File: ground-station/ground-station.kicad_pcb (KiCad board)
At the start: 2 copper layers, 60 parts, among them J1 Conn_01x02, J10 Conn_01x02, J2 Conn_01x02, J3 Conn_01x02, J4 Conn_01x02, J5 Conn_01x05, J6 Conn_01x04, J7 USB_B_Micro, J8 Conn_01x02, J9 Conn_01x02, SW1 SW_Push, U1 LM3940, U2 STM32F401RETx, U3 RFM69HCW

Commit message: lots of work on layout + change button to compact button
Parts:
- removed TP5, TP6: TestPoint, TestPoint:TestPoint_THTPad_1.0x1.0mm_Drill0.5mm
- added REF**: MountingHole_3.2mm_M3_ISO14580_Pad, MountingHole:MountingHole_3.2mm_M3_ISO14580_Pad, F.Cu at (156.2, 29.5)
- C1, C10, C11, C12, C2, C3, C4, C5, C6, C7, C8, C9, F1, R1, R2, R7, U1, U2: moved to B.Cu
- SW1: footprint Button_Switch_THT:SW_PUSH_6mm -> calstar:TE_Button_USLPT3026
- TP1, TP10, TP11, TP12, TP13, TP14, TP15, TP16, TP17, TP18, TP19, TP2, TP20, TP21, TP3, TP4, TP7, TP8, TP9: footprint TestPoint:TestPoint_THTPad_1.0x1.0mm_Drill0.5mm -> TestPoint:TestPoint_THTPad_D1.0mm_Drill0.5mm
- moved J5 236.2 mm to (220.5, 48.0), turned to 270 degrees
- moved J7 226.1 mm to (220.2, 35.2), turned to 90 degrees
- moved D1 213.2 mm to (214.9, 41.1)
- moved J8 208.0 mm to (212.9, 39.1)
- moved J6 205.0 mm to (208.0, 27.9), turned to 90 degrees
- moved TP14 204.6 mm to (216.9, 45.0)
- moved SW1 204.5 mm to (196.1, 27.4), turned to 180 degrees
- moved U1 203.6 mm to (212.9, 35.6), turned to 90 degrees
- moved C1 201.8 mm to (214.9, 41.1), turned to 180 degrees
- moved R6 199.7 mm to (201.3, 37.6)
- moved J1 199.4 mm to (201.9, 42.9)
- moved R3 198.1 mm to (215.3, 42.9), turned to 180 degrees
- moved TP3 196.9 mm to (212.6, 43.2)
- moved F1 194.9 mm to (218.6, 41.1)
- moved TP2 194.2 mm to (220.7, 42.9), turned to 90 degrees
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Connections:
- AE1 pad 1: GND -> /RFM69HCW/ANT
- AE1 pad 2: /RFM69HCW/ANT -> GND
- J1 pad : (no net) -> GND
- J10 pad : (no net) -> GND
- J2 pad : (no net) -> GND
- J3 pad : (no net) -> GND
- J4 pad : (no net) -> GND
- J5 pad 1: +3V3 -> GND
- J5 pad 2: SWO -> SWCLK
- J5 pad 4: SWCLK -> SWO
- J5 pad 5: GND -> +3V3
- J6 pad 1: +5V -> GND
- J6 pad 4: GND -> +5V
- J8 pad : (no net) -> GND
- J9 pad : (no net) -> GND
- R1 pad 1: Net-(J6-Pad2) -> Net-(J6-Pad3)
- R2 pad 1: Net-(J6-Pad3) -> Net-(J6-Pad2)
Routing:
- net +3V3: track 0.00 -> 116.8 mm, vias 0 -> 4
- net GND: track 0.00 -> 63.1 mm, vias 0 -> 4
- net RadioINT: track 0.00 -> 40.3 mm
- net +5V: track 0.00 -> 36.5 mm, vias 0 -> 2
- net RadioMISO: track 0.00 -> 35.8 mm
- net RadioMOSI: track 0.00 -> 34.1 mm
- net RadioSCK: track 0.00 -> 29.1 mm
- net nRST: track 0.00 -> 27.5 mm
- net RadionSS: track 0.00 -> 23.6 mm
- net SWCLK: track 0.00 -> 18.2 mm
- net OTG_FS_D-: track 0.00 -> 17.7 mm, vias 0 -> 1
- net OTG_FS_D+: track 0.00 -> 17.1 mm, vias 0 -> 1
- net SWO: track 0.00 -> 17.0 mm
- net RadioRST: track 0.00 -> 15.7 mm
- net SWDIO: track 0.00 -> 14.3 mm
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- added copper zone on B.Cu, net GND
- added copper zone on F.Cu, net GND
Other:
- board outline added: 69.8 x 31.8 mm
- net class Default: trace_width 0.25 -> 0.1778
- net class Power added: clearance 0.2, trace_width 0.254, via_dia 0.8, via_drill 0.4
- rule trace_min: 0.2 -> 0.1524

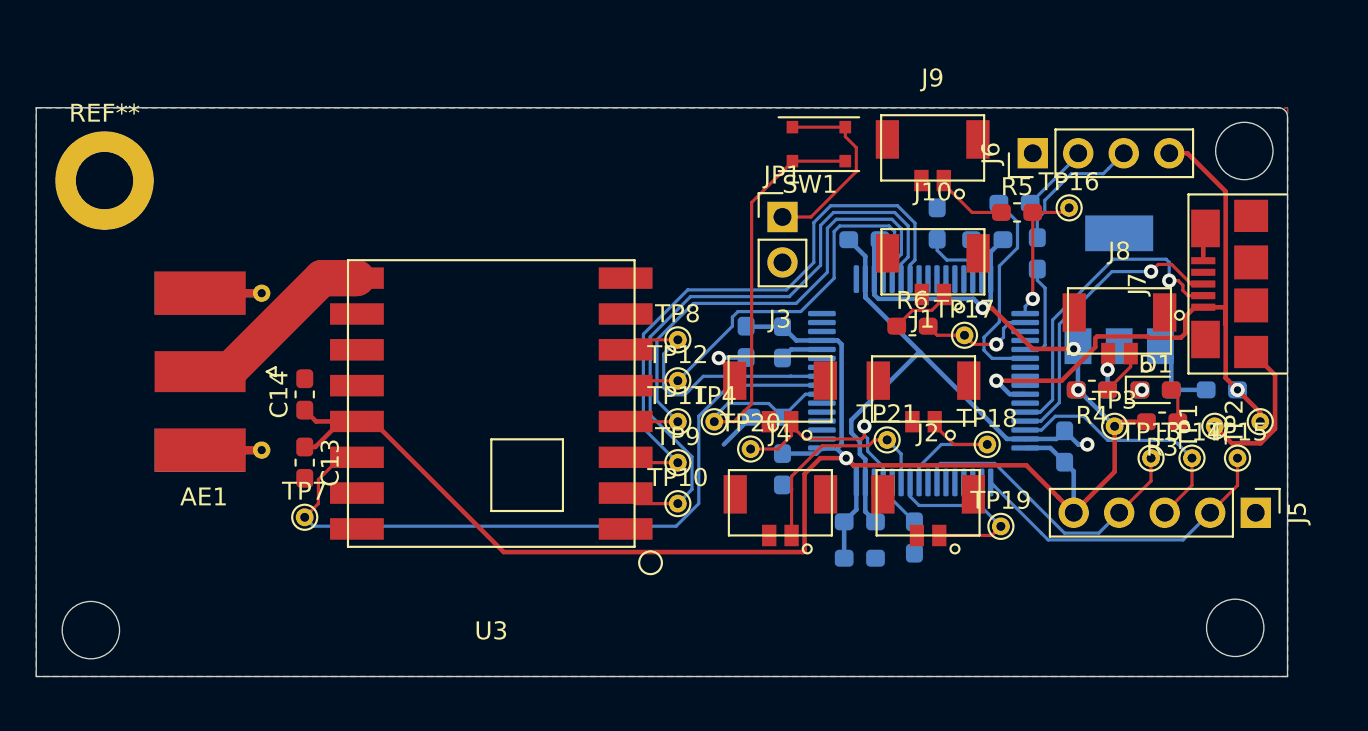
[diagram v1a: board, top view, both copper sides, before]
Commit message: mounting holes, more uniform connectors
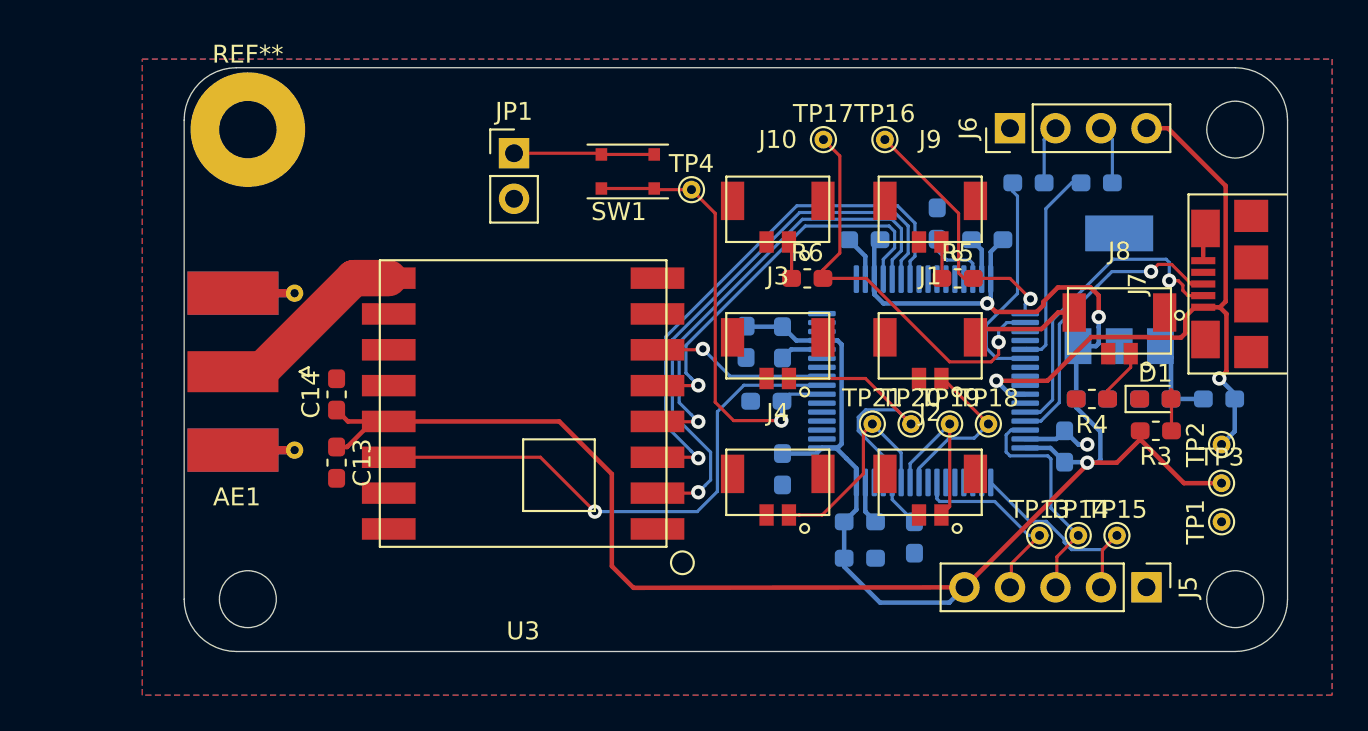
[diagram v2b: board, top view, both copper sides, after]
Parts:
- removed the REF** at (156.2, 29.5)
- removed TP10, TP11, TP12, TP7, TP8, TP9: TestPoint, TestPoint:TestPoint_THTPad_D1.0mm_Drill0.5mm
- added REF**: MountingHole_3.2mm_M3_Pad, MountingHole:MountingHole_3.2mm_M3_Pad, F.Cu at (164.2, 26.6)
- moved JP1 15.4 mm to (179.1, 27.9)
- moved TP17 13.5 mm to (196.3, 27.2)
- moved TP4 13.0 mm to (189.0, 30.0)
- moved TP16 11.0 mm to (199.8, 27.2)
- moved SW1 10.8 mm to (185.4, 29.0)
- moved J10 9.14 mm to (193.8, 32.9)
- moved TP20 9.06 mm to (201.2, 43.1)
- moved TP15 8.00 mm to (212.7, 49.3)
- moved TP14 7.68 mm to (210.6, 49.3)
- moved TP13 7.57 mm to (208.4, 49.3)
- moved J5 7.38 mm to (214.4, 52.2)
- moved TP3 6.76 mm to (218.6, 46.4)
- moved R6 6.45 mm to (195.4, 34.9)
- moved TP19 6.39 mm to (203.4, 43.1)
- moved TP1 5.35 mm to (218.6, 48.5)
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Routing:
- net GND: track 63.1 -> 29.9 mm, vias 4 -> 1
- net LED2: track 6.63 -> 23.5 mm
- net +3V3: track 116.8 -> 133.1 mm, vias 4 -> 3
- net RadioINT: track 40.3 -> 31.0 mm, vias 0 -> 1
- net LED1: track 7.96 -> 14.7 mm
- net SWCLK: track 18.2 -> 12.3 mm
- net RadioRST: track 15.7 -> 9.83 mm, vias 0 -> 1
- net MCU_TX: track 5.73 -> 11.5 mm
- net SWO: track 17.0 -> 11.7 mm
- net Net-(J6-Pad3): track 7.87 -> 3.31 mm
- net RadioMISO: track 35.8 -> 31.5 mm, vias 0 -> 1
- net RadioMOSI: track 34.1 -> 30.4 mm, vias 0 -> 1
- net RadioSCK: track 29.1 -> 25.6 mm, vias 0 -> 1
- net IO3: track 12.2 -> 15.5 mm, vias 1 -> 0
- net Net-(JP1-Pad1): track 10.9 -> 7.96 mm
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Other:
- board size 69.8 x 31.8 mm -> 61.6 x 32.6 mm

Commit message: silkscreen
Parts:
- removed SW1: SW_Push, calstar:TE_Button_USLPT3026
- removed TP14: TestPoint, TestPoint:TestPoint_THTPad_D1.0mm_Drill0.5mm
- added SW RST: SW_Push, calstar:TE_Button_USLPT3026, F.Cu at (190.2, 52.6)
- added SWDIO: TestPoint, TestPoint:TestPoint_THTPad_D1.0mm_Drill0.5mm, F.Cu at (209.3, 49.3)
- Mounting Hole: renamed from REF**
- moved JP1 25.3 mm to (184.2, 52.7), turned to 270 degrees
- moved nRST 24.0 mm to (194.1, 53.4)
- moved R4 6.77 mm to (210.6, 34.9)
- moved J8 6.56 mm to (210.8, 32.9)
- moved SWO 1.65 mm to (206.8, 49.3)
- moved SWCLK 0.89 mm to (211.8, 49.3)
- renumbered TP3 to +3V3, TP2 to +5V, TP1 to GND, TP18 to IO1, TP19 to IO2, TP20 to IO3, TP21 to IO4, TP16 to LED1, TP17 to LED2, TP15 to SWCLK, TP13 to SWO, TP4 to nRST
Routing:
- net nRST: track 25.2 -> 20.4 mm, vias 1 -> 3
- net OTG_FS_D-: track 17.7 -> 13.2 mm
- net +3V3: track 133.1 -> 129.5 mm
- net GND: track 29.9 -> 27.0 mm, vias 1 -> 3
- net SWO: track 11.7 -> 9.40 mm
- net SWDIO: track 13.7 -> 11.6 mm
- net OTG_FS_D+: track 17.1 -> 15.2 mm
- net +5V: track 38.0 -> 36.5 mm
- net Net-(J8-Pad1): track 3.26 -> 2.08 mm
- net SWCLK: track 12.3 -> 13.0 mm
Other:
- board text added: "+3V3 SWO SWDIO SWCLK GND"
- board text added: "+5V TX RX GND"
- board text added: "IO2"

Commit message: changes from first review from aled and rajiv
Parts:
- C2: value 33uF -> 47uF
- SW1: renamed from SW RST
- renumbered GND to TP1, SWO to TP13, SWDIO to TP14, SWCLK to TP15, LED1 to TP16, LED2 to TP17, IO1 to TP18, IO2 to TP19, +5V to TP2, IO3 to TP20, IO4 to TP21, +3V3 to TP3, nRST to TP4
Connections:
- U2 pad 42: +5V -> /STM32F401RET6/PA9
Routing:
- net GND: track 27.0 -> 41.1 mm, vias 3 -> 37
- net +5V: track 36.5 -> 23.3 mm, vias 2 -> 1
- net Net-(C1-Pad1): track 5.89 -> 5.00 mm
- net Net-(D1-Pad2): track 2.51 -> 1.79 mm
- net RadioINT: track 31.0 -> 31.6 mm
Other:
- net class Power: trace_width 0.254 -> 0.3556
- board text added: "+3V3"
- board text added: "+5V"
- board text added: "GND"
- board text added: "IO1"
- board text added: "IO3"
- board text added: "IO4"
- board text added: "LED1"
- board text added: "LED2"
- board text added: "SWCLK"
- board text added: "SWDIO"
- board text added: "SWO"
- board text added: "nRST"

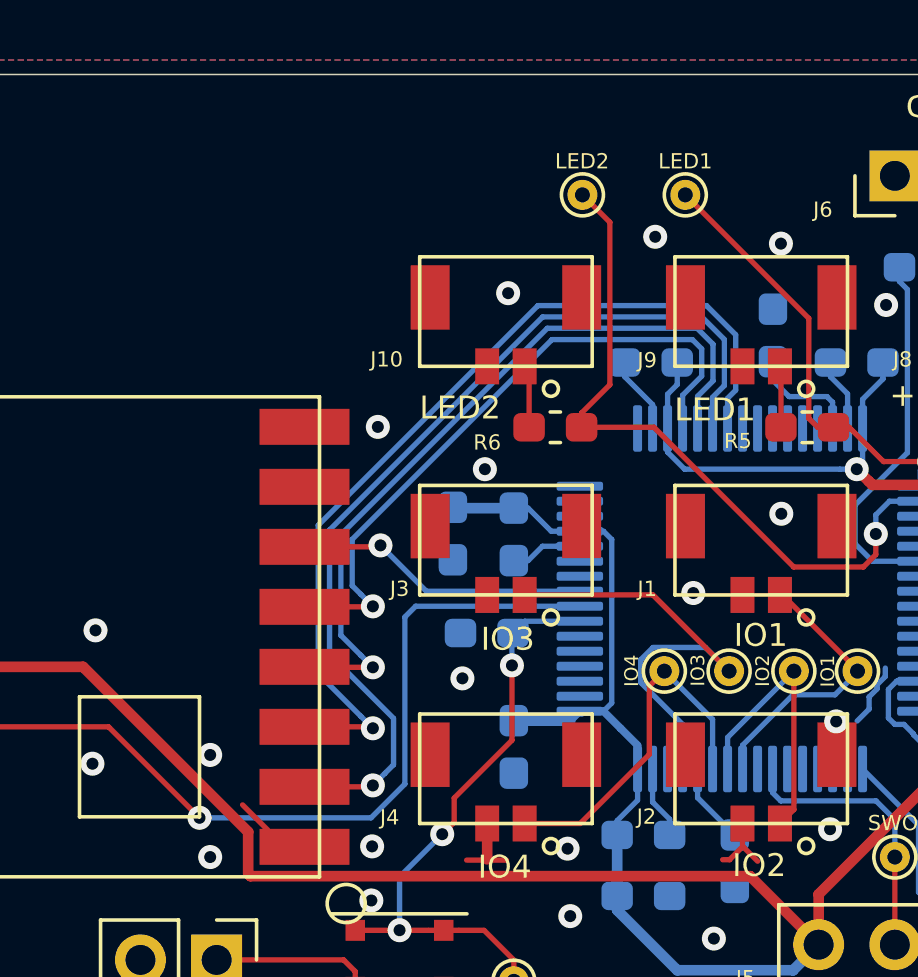
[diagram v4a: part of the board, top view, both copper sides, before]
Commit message: shorted radio SPI traces on back layer
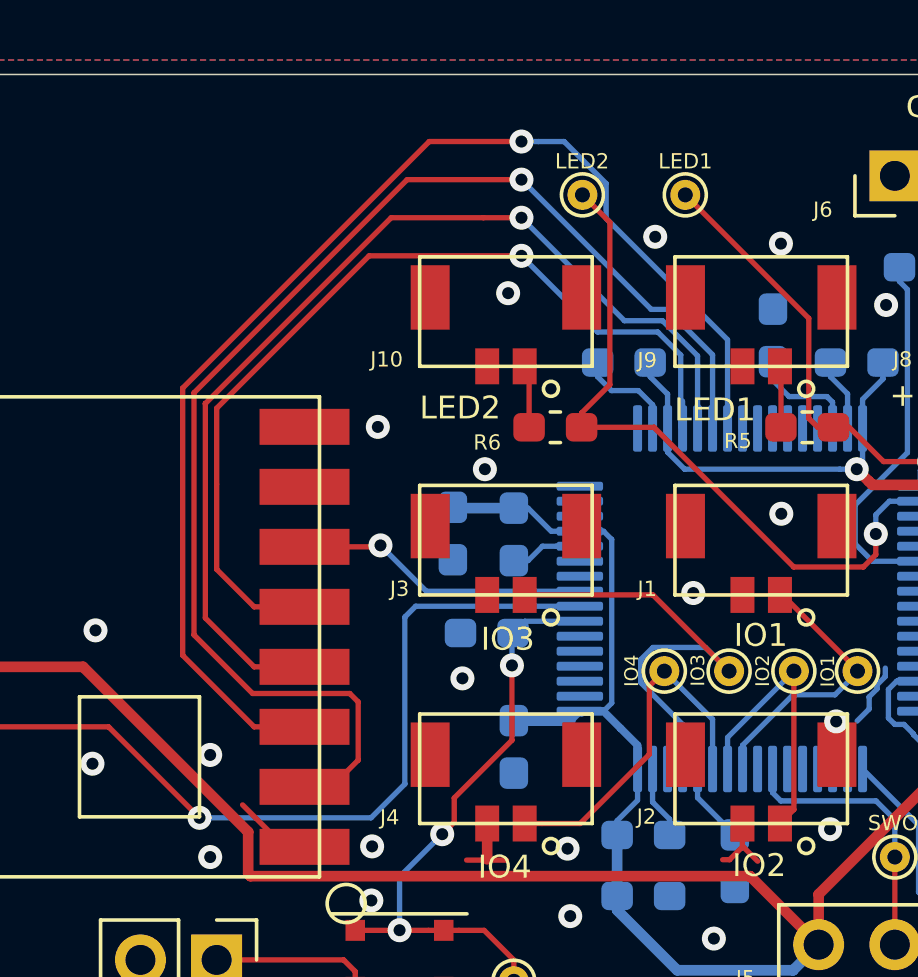
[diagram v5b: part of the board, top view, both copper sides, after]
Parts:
- moved C12 0.90 mm to (197.7, 32.8)
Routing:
- net RadioMISO: track 31.5 -> 44.7 mm
- net RadioMOSI: track 30.4 -> 41.9 mm
- net RadionSS: track 22.3 -> 31.1 mm
- net RadioSCK: track 25.6 -> 34.5 mm
- net GND: track 41.1 -> 42.0 mm
